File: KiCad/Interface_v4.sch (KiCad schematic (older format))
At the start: 22 parts, among them J501 IR LED, Q501 NTR4003N, U501 WS2812B, U502 WS2812B, U503 WS2812B

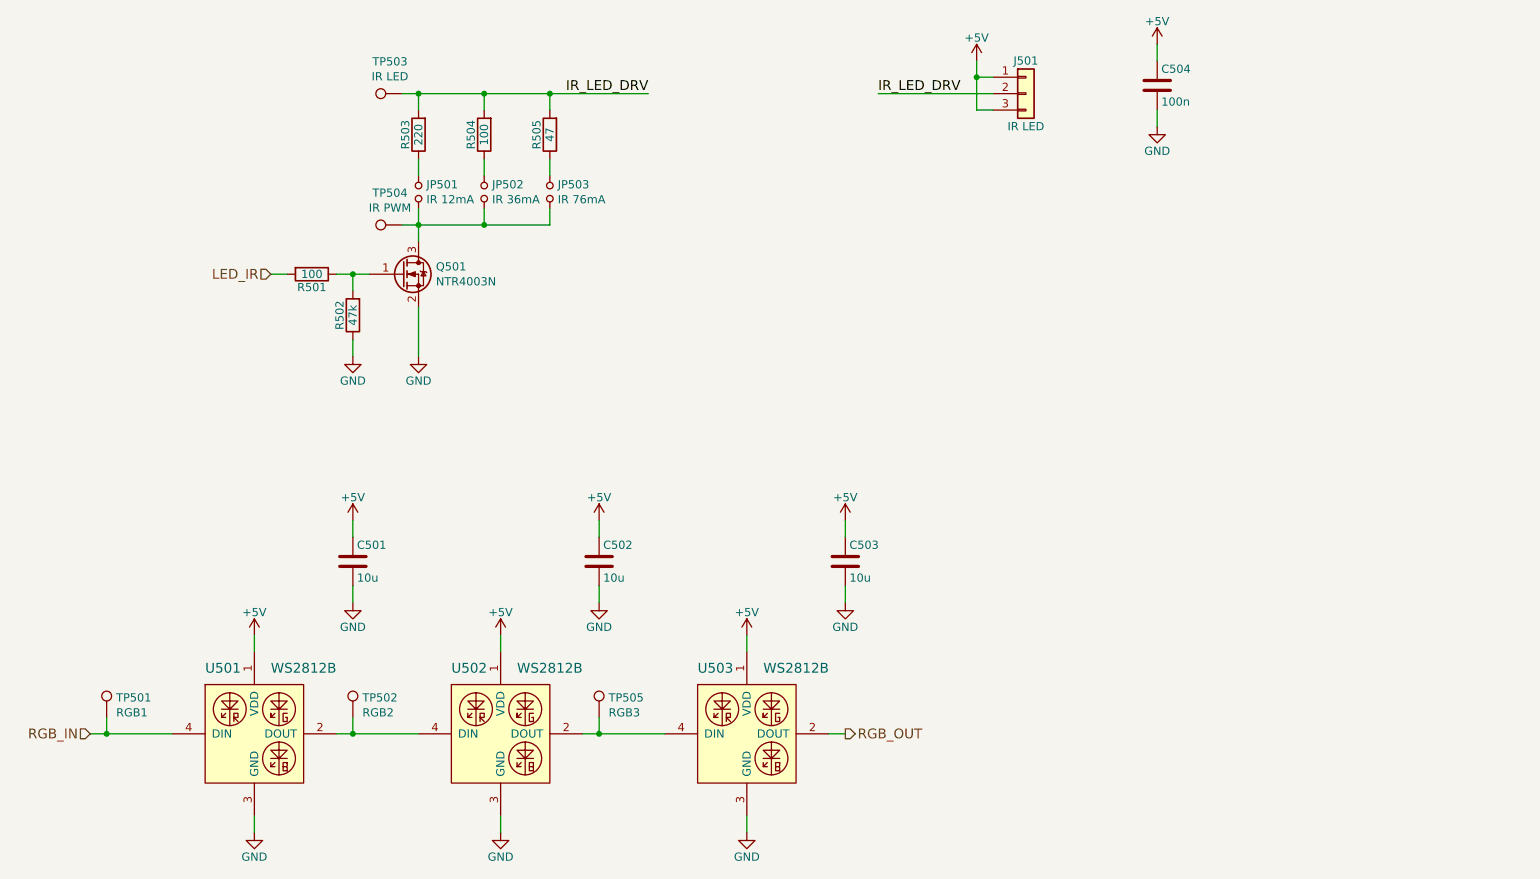
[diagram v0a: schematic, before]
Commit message: Version 4 Shift Register
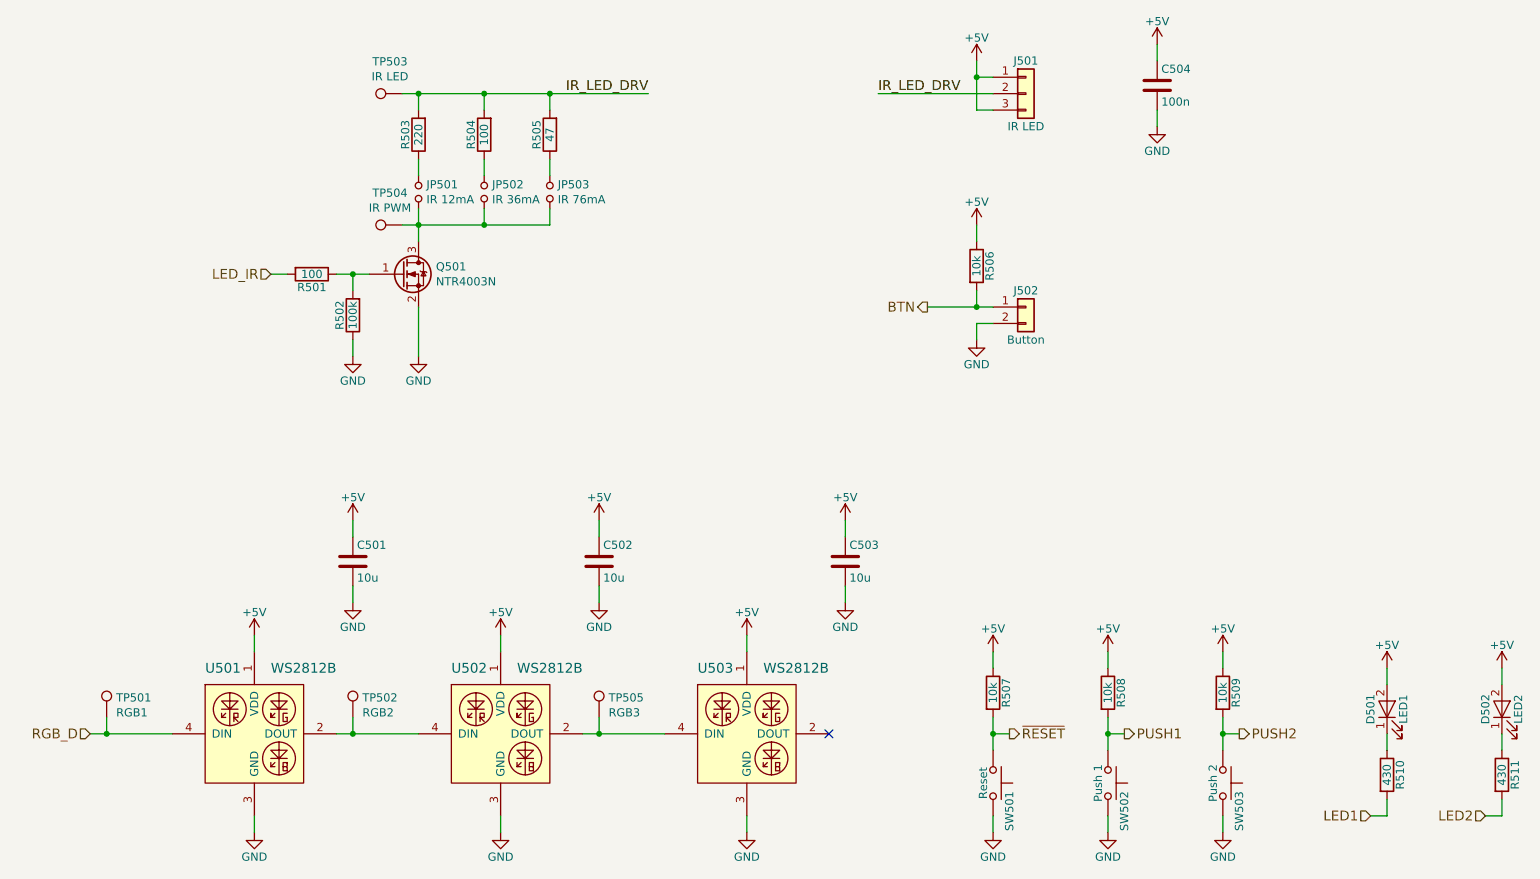
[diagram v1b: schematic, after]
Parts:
- added D501: LED1, LEDs:LED_D3.0mm, symbol LED
- added D502: LED2, LEDs:LED_D3.0mm, symbol LED
- added J502: Button, Connectors_Molex:Molex_KK-6410-02_02x2.54mm_Straight, symbol Conn_01x02
- added R506, R507, R508, R509: 10k, Resistors_SMD:R_0805, symbol R
- added R510, R511: 430, Resistors_SMD:R_0805, symbol R
- added SW501: Reset, Buttons_Switches_THT:SW_PUSH_6mm_h5mm, symbol SW_Push
- added SW502: Push 1, Buttons_Switches_THT:SW_PUSH_6mm_h5mm, symbol SW_Push
- added SW503: Push 2, Buttons_Switches_THT:SW_PUSH_6mm_h5mm, symbol SW_Push
- Q501: Alternative Logic Level N-ch 500mA MOS (PMBF170) -> Logic Level N-ch 500mA MOS
- R502: value 47k -> 100k
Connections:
- net +5V: now also D501.2 (A), D502.2 (A), R506.1, R507.1, R508.1, R509.1
- net GND: now also J502.2 (Pin_2), SW501.2, SW502.2, SW503.2
- net RGB_IN renamed RGB_D
- net RGB_OUT: no longer names the net of U503.2 (DOUT)
- new net: D501.1 (K), R510.1
- new net: D502.1 (K), R511.1
- new net BTN: J502.1 (Pin_1), R506.2
- new net LED1: R510.2
- new net LED2: R511.2
- new net PUSH1: R508.2, SW502.1
- new net PUSH2: R509.2, SW503.1
- new net ~RESET: R507.2, SW501.1
- no-connect marks 0 -> 1
